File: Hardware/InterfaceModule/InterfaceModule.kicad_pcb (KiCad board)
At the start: 2 copper layers, 25 parts, among them J1 External GPS IN, J13 TS-480 COM, J14 TS-480 COM, J15 External COM, J2 External GPS OUT, J3 D-700 GPS, J4 External MIC IN, J5 D-700 MIC, J6 TS-480 MIC, J7 D-700 EXT.SP 1, J8 TS-480 EXT.SP, K1 4PDT Relay, K10 3PDT Relay, K11 3PDT Relay, K12 3PDT Relay, K13 3PDT Relay, K14 3PDT Relay, K2 4PDT Relay, K3 4PDT Relay, K4 4PDT Relay, K5 3PDT Relay, K6 3PDT Relay, K7 3PDT Relay, K8 3PDT Relay, K9 3PDT Relay

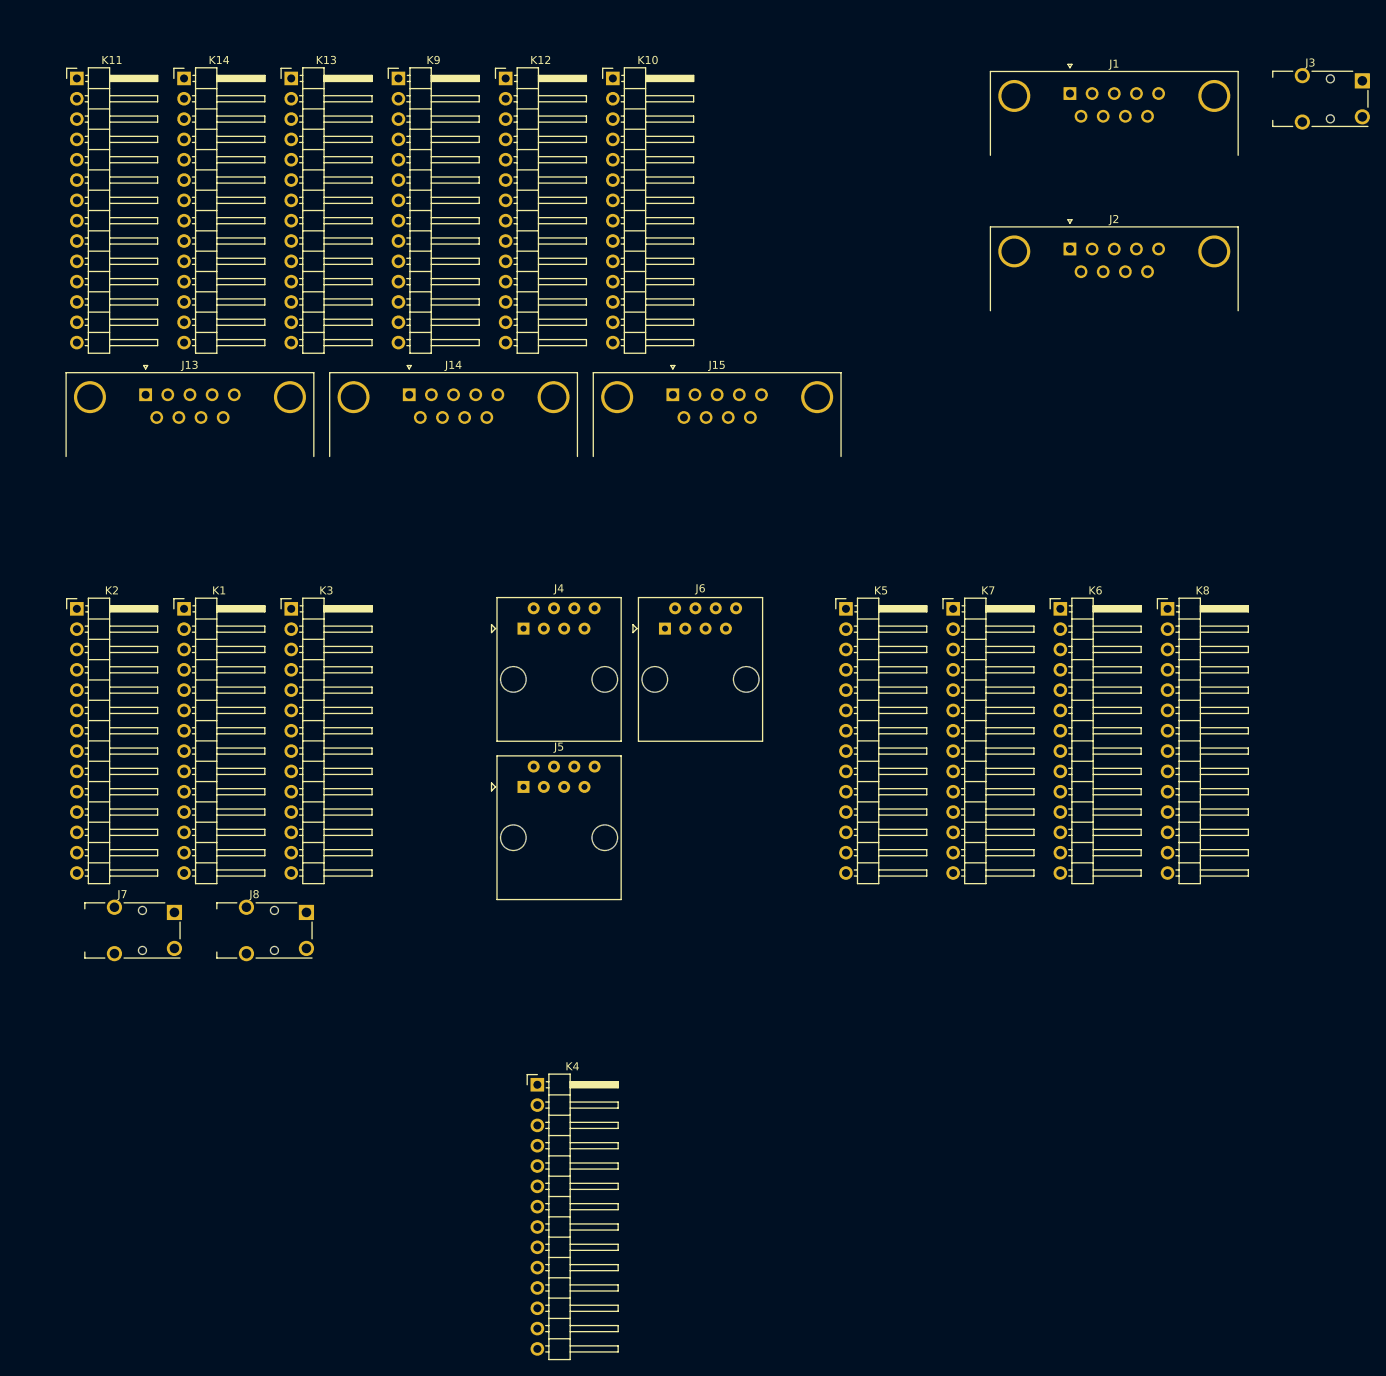
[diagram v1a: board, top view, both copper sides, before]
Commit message: Added selector input
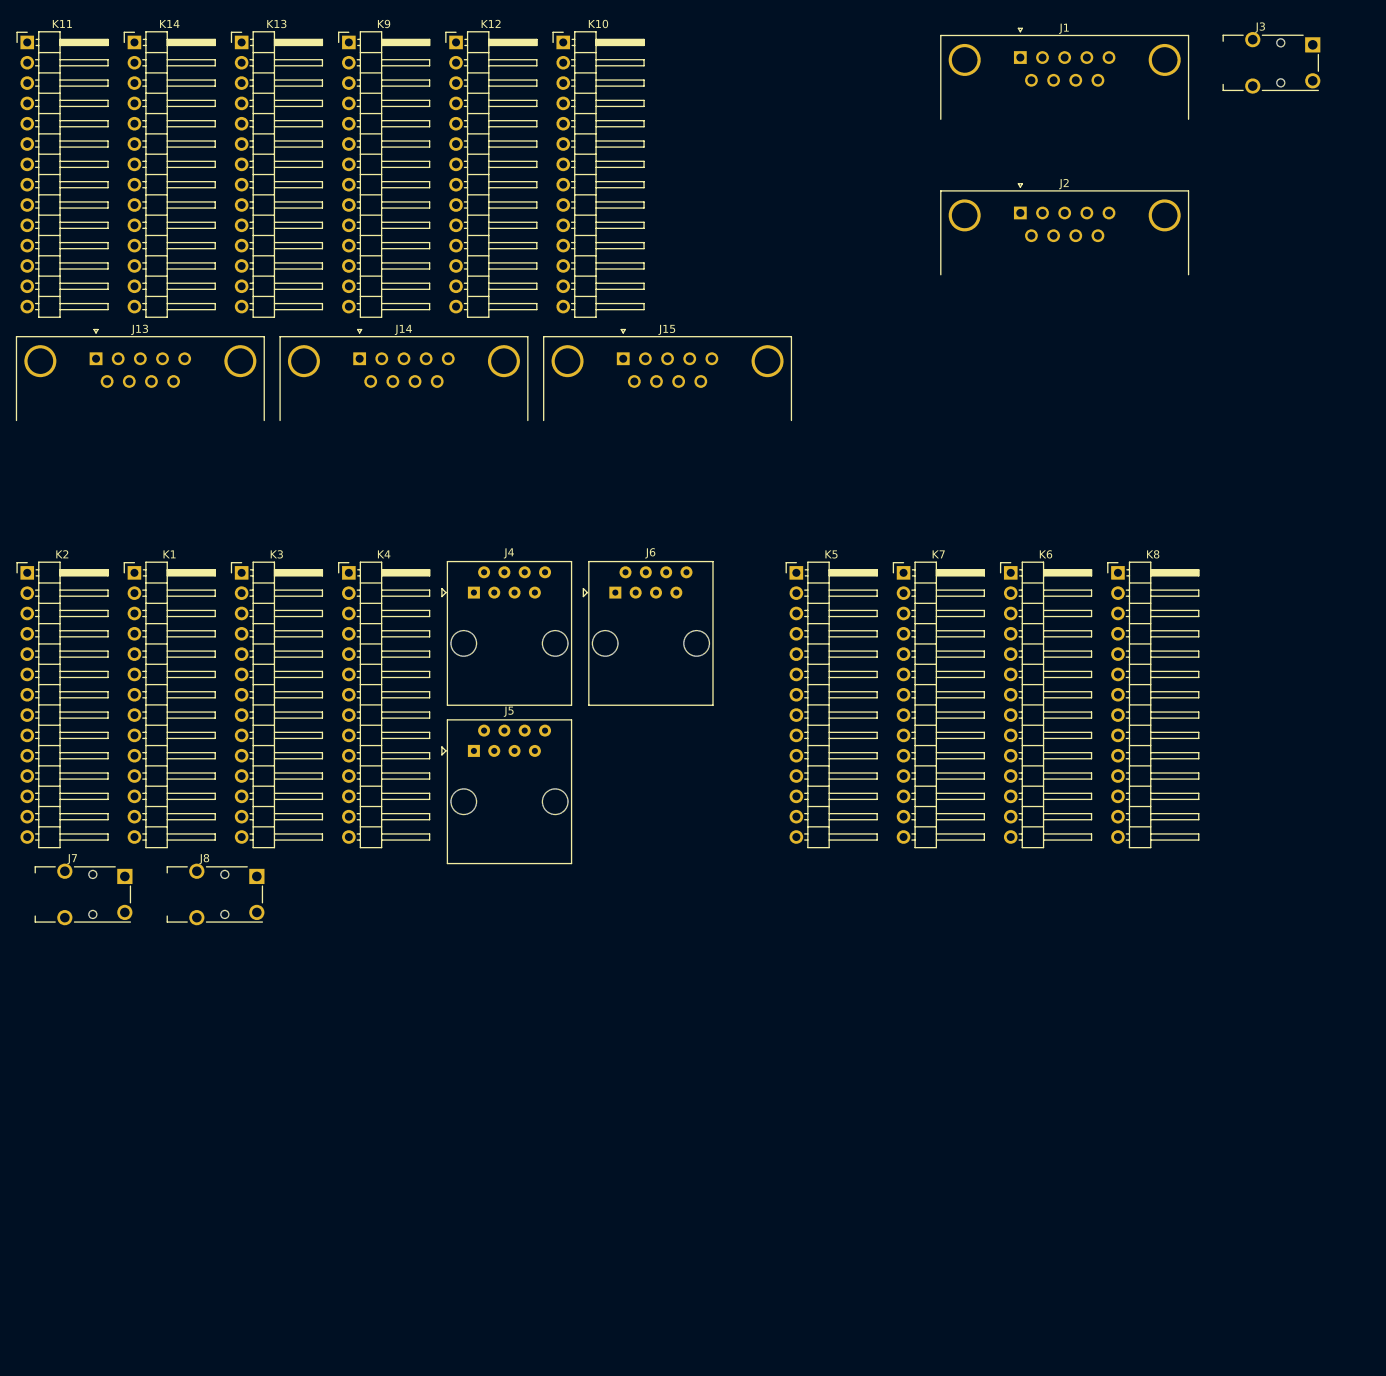
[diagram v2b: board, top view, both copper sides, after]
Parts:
- removed the J13 at (67.5, 88.5)
- added J14: TS-480 COM, Connector_Dsub:DSUB-9_Male_Horizontal_P2.77x2.84mm_EdgePinOffset4.94mm_Housed_MountingHolesOffset7.48mm, F.Cu at (94.2, 84.0)
- moved K4 68.2 mm to (92.9, 110.8)
- moved J13 39.4 mm to (61.3, 84.0)
- moved J15 7.66 mm to (127.2, 84.0)
- moved J3 7.66 mm to (206.8, 47.1)
- moved K6 7.66 mm to (175.6, 110.8)
- moved K7 7.66 mm to (162.2, 110.8)
- moved J6 7.66 mm to (126.2, 113.3)
- moved J7 7.66 mm to (58.4, 151.0)
- moved J8 7.66 mm to (74.9, 151.0)
- moved K1 7.66 mm to (66.1, 110.8)
- moved K10 7.66 mm to (119.7, 44.5)
- moved K11 7.66 mm to (52.7, 44.5)
- moved K13 7.66 mm to (79.5, 44.5)
- moved K14 7.66 mm to (66.1, 44.5)
- moved K2 7.66 mm to (52.7, 110.8)
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- renumbered J14 to J13
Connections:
- net /Data Port Switching/DATA_ANG renamed /Data Port Switching/480_DATA_ANG
- net /Data Port Switching/DATA_ANI renamed /Data Port Switching/480_DATA_ANI
- net /Data Port Switching/DATA_ANO renamed /Data Port Switching/480_DATA_ANO
- net /Data Port Switching/DATA_DE renamed /Data Port Switching/D700_DATA_DE
- net /Data Port Switching/DATA_DTS renamed /Data Port Switching/480_DATA_DTS
- net /Data Port Switching/DATA_NC renamed /Data Port Switching/480_DATA_NC
- net /Data Port Switching/DATA_PKD renamed /Data Port Switching/D700_DATA_PKD
- net /Data Port Switching/DATA_PKS renamed /Data Port Switching/D700_DATA_PKS
- net /Data Port Switching/DATA_PR1 renamed /Data Port Switching/D700_DATA_PR1
- net /Data Port Switching/DATA_PR9 renamed /Data Port Switching/D700_DATA_PR9
- J13 pad 1: /COM Port Switching/NC1 -> /COM Port Switching/480_NC1
- J13 pad 2: /COM Port Switching/RX -> /COM Port Switching/480_RX
- J13 pad 3: /COM Port Switching/TX -> /COM Port Switching/480_TX
- J13 pad 4: /COM Port Switching/DTR -> /COM Port Switching/480_DTR
- J13 pad 5: GND -> /COM Port Switching/480_GND
- J13 pad 6: /COM Port Switching/DSR -> /COM Port Switching/480_DSR
- J13 pad 7: /COM Port Switching/RTS -> /COM Port Switching/480_RTS
- J13 pad 8: /COM Port Switching/CTS -> /COM Port Switching/480_CTS
- J13 pad 9: /COM Port Switching/NC2 -> /COM Port Switching/480_NC2
- J15 pad 1: /COM Port Switching/NC1 -> /COM Port Switching/EXT_NC1
- J15 pad 2: /COM Port Switching/RX -> /COM Port Switching/EXT_RX
- J15 pad 3: /COM Port Switching/TX -> /COM Port Switching/EXT_TX
- J15 pad 4: /COM Port Switching/DTR -> /COM Port Switching/EXT_DTR
- J15 pad 5: GND -> /COM Port Switching/EXT_GND
- J15 pad 6: /COM Port Switching/DSR -> /COM Port Switching/EXT_DSR
- J15 pad 7: /COM Port Switching/RTS -> /COM Port Switching/EXT_RTS
- J15 pad 8: /COM Port Switching/CTS -> /COM Port Switching/EXT_CTS
- J15 pad 9: /COM Port Switching/NC2 -> /COM Port Switching/EXT_NC2
- J4 pad 1: /Microphone Switching/UP -> /Microphone Switching/EXT_UP
- J4 pad 2: /Microphone Switching/8V -> /Microphone Switching/EXT_8V
- J4 pad 3: GND -> /Microphone Switching/EXT_GND
- J4 pad 4: /Microphone Switching/PTT -> /Microphone Switching/EXT_PTT
- J4 pad 5: /Microphone Switching/MICGND -> /Microphone Switching/EXT_MICGND
- J4 pad 6: /Microphone Switching/MIC -> /Microphone Switching/EXT_MIC
- J4 pad 7: /Microphone Switching/NC -> /Microphone Switching/EXT_NC
- J4 pad 8: /Microphone Switching/DWN -> /Microphone Switching/EXT_DWN
- J5 pad 1: /Microphone Switching/UP -> /Microphone Switching/D700_UP
- J5 pad 2: /Microphone Switching/8V -> /Microphone Switching/D700_8V
- J5 pad 3: GND -> /Microphone Switching/D700_GND
- J5 pad 4: /Microphone Switching/PTT -> /Microphone Switching/D700_PTT
- J5 pad 5: /Microphone Switching/MICGND -> /Microphone Switching/D700_MICGND
- J5 pad 6: /Microphone Switching/MIC -> /Microphone Switching/D700_MIC
- J5 pad 7: /Microphone Switching/NC -> /Microphone Switching/D700_NC
- J5 pad 8: /Microphone Switching/DWN -> /Microphone Switching/D700_DWN
- J6 pad 1: /Microphone Switching/UP -> /Microphone Switching/480_UP
- J6 pad 2: /Microphone Switching/8V -> /Microphone Switching/480_8V
- J6 pad 3: GND -> /Microphone Switching/480_GND
- J6 pad 4: /Microphone Switching/PTT -> /Microphone Switching/480_PTT
- J6 pad 5: /Microphone Switching/MICGND -> /Microphone Switching/480_MICGND
- J6 pad 6: /Microphone Switching/MIC -> /Microphone Switching/480_MIC
- J6 pad 7: /Microphone Switching/NC -> /Microphone Switching/480_NC
- J6 pad 8: /Microphone Switching/DWN -> /Microphone Switching/480_DWN
- J7 pad S: /Microphone Switching/SP_S -> /Microphone Switching/D700_SP_S
- J7 pad T: /Microphone Switching/SP_T -> /Microphone Switching/D700_SP_T
- J8 pad S: /Microphone Switching/SP_S -> /Microphone Switching/480_SP_S
- J8 pad T: /Microphone Switching/SP_T -> /Microphone Switching/480_SP_T
- K1 pad 11: /Microphone Switching/UP -> /Microphone Switching/D700_UP
- K1 pad 12: /Microphone Switching/8V -> /Microphone Switching/D700_8V
- K1 pad 13: GND -> /Microphone Switching/D700_GND
- K1 pad 14: /Microphone Switching/PTT -> /Microphone Switching/D700_PTT
- K1 pad 2: /Microphone Switching/UP -> /Microphone Switching/EXT_UP
- K1 pad 4: /Microphone Switching/8V -> /Microphone Switching/EXT_8V
- K1 pad 6: GND -> /Microphone Switching/EXT_GND
- K1 pad 8: /Microphone Switching/PTT -> /Microphone Switching/EXT_PTT
- K10 pad 2: /COM Port Switching/DTR -> /COM Port Switching/D700_DTR
- K10 pad 3: /COM Port Switching/DSR -> /COM Port Switching/EXT_DSR
- K10 pad 4: /COM Port Switching/DSR -> /COM Port Switching/D700_DSR
- K10 pad 5: /COM Port Switching/DTR -> /COM Port Switching/EXT_DTR
- K10 pad 6: /COM Port Switching/RX -> /COM Port Switching/D700_RX
- K10 pad 7: /COM Port Switching/TX -> /COM Port Switching/EXT_TX
- K11 pad 2: /COM Port Switching/CTS -> /COM Port Switching/480_CTS
- K11 pad 3: /COM Port Switching/RTS -> /COM Port Switching/EXT_RTS
- K11 pad 4: /COM Port Switching/RX -> /COM Port Switching/480_RX
- K11 pad 5: /COM Port Switching/TX -> /COM Port Switching/EXT_TX
- K11 pad 6: /COM Port Switching/RTS -> /COM Port Switching/480_RTS
- K11 pad 7: /COM Port Switching/CTS -> /COM Port Switching/EXT_CTS
- K12 pad 2: /COM Port Switching/RTS -> /COM Port Switching/D700_RTS
- K12 pad 3: /COM Port Switching/CTS -> /COM Port Switching/EXT_CTS
- K12 pad 4: /COM Port Switching/TX -> /COM Port Switching/D700_TX
- K12 pad 5: /COM Port Switching/RX -> /COM Port Switching/EXT_RX
- K12 pad 6: /COM Port Switching/CTS -> /COM Port Switching/D700_CTS
- K12 pad 7: /COM Port Switching/RTS -> /COM Port Switching/EXT_RTS
- K13 pad 2: /COM Port Switching/NC1 -> /COM Port Switching/480_NC1
- K13 pad 3: /COM Port Switching/NC1 -> /COM Port Switching/EXT_NC1
- K13 pad 4: /COM Port Switching/NC2 -> /COM Port Switching/480_NC2
- K13 pad 5: /COM Port Switching/NC2 -> /COM Port Switching/EXT_NC2
- K13 pad 6: GND -> /COM Port Switching/480_GND
- K13 pad 7: GND -> /COM Port Switching/EXT_GND
- K14 pad 2: /COM Port Switching/NC1 -> /COM Port Switching/D700_NC1
- K14 pad 3: /COM Port Switching/NC1 -> /COM Port Switching/EXT_NC1
- K14 pad 4: /COM Port Switching/NC2 -> /COM Port Switching/D700_NC2
- K14 pad 5: /COM Port Switching/NC2 -> /COM Port Switching/EXT_NC2
- K14 pad 6: GND -> /COM Port Switching/D700_GND
- K14 pad 7: GND -> /COM Port Switching/EXT_GND
- K2 pad 11: /Microphone Switching/PTT -> /Microphone Switching/480_PTT
- K2 pad 12: GND -> /Microphone Switching/480_GND
- K2 pad 13: /Microphone Switching/8V -> /Microphone Switching/480_8V
- K2 pad 14: /Microphone Switching/UP -> /Microphone Switching/480_UP
- K2 pad 3: /Microphone Switching/PTT -> /Microphone Switching/EXT_PTT
- K2 pad 5: GND -> /Microphone Switching/EXT_GND
- K2 pad 7: /Microphone Switching/8V -> /Microphone Switching/EXT_8V
- K2 pad 9: /Microphone Switching/UP -> /Microphone Switching/EXT_UP
- K3 pad 11: /Microphone Switching/MICGND -> /Microphone Switching/D700_MICGND
- K3 pad 12: /Microphone Switching/MIC -> /Microphone Switching/D700_MIC
- K3 pad 13: /Microphone Switching/NC -> /Microphone Switching/D700_NC
- K3 pad 14: /Microphone Switching/DWN -> /Microphone Switching/D700_DWN
- K3 pad 2: /Microphone Switching/MICGND -> /Microphone Switching/EXT_MICGND
- K3 pad 3: /Microphone Switching/SP_T -> /Microphone Switching/480_SP_T
- K3 pad 4: /Microphone Switching/MIC -> /Microphone Switching/EXT_MIC
- K3 pad 6: /Microphone Switching/NC -> /Microphone Switching/EXT_NC
- K3 pad 8: /Microphone Switching/DWN -> /Microphone Switching/EXT_DWN
- K4 pad 11: /Microphone Switching/DWN -> /Microphone Switching/480_DWN
- K4 pad 12: /Microphone Switching/NC -> /Microphone Switching/480_NC
- K4 pad 13: /Microphone Switching/MIC -> /Microphone Switching/480_MIC
- K4 pad 14: /Microphone Switching/MICGND -> /Microphone Switching/480_MICGND
- K4 pad 3: /Microphone Switching/DWN -> /Microphone Switching/EXT_DWN
- K4 pad 5: /Microphone Switching/NC -> /Microphone Switching/EXT_NC
- K4 pad 7: /Microphone Switching/MIC -> /Microphone Switching/EXT_MIC
- K4 pad 8: /Microphone Switching/SP_T -> /Microphone Switching/D700_SP_T
- K4 pad 9: /Microphone Switching/MICGND -> /Microphone Switching/EXT_MICGND
- K5 pad 3: /Data Port Switching/RADIO_4 -> /Data Port Switching/SignaLink2_RADIO_4
- K5 pad 5: /Data Port Switching/RADIO_1 -> /Data Port Switching/SignaLink2_RADIO_1
- K5 pad 7: /Data Port Switching/RADIO_5 -> /Data Port Switching/SignaLink2_RADIO_5
- K6 pad 3: /Data Port Switching/RADIO_0 -> /Data Port Switching/SignaLink1_RADIO_0
- K6 pad 5: /Data Port Switching/RADIO_1 -> /Data Port Switching/SignaLink1_RADIO_1
- K6 pad 6: /Data Port Switching/DATA_SQC -> /Data Port Switching/D700_DATA_SQC
- K6 pad 7: /Data Port Switching/RADIO_2 -> /Data Port Switching/SignaLink1_RADIO_2
- K7 pad 3: /Data Port Switching/RADIO_3 -> /Data Port Switching/SignaLink2_RADIO_3
- K7 pad 5: /Data Port Switching/RADIO_0 -> /Data Port Switching/SignaLink2_RADIO_0
- K7 pad 6: /Data Port Switching/DATA_SQC -> /Data Port Switching/480_DATA_SQC
- K7 pad 7: /Data Port Switching/RADIO_2 -> /Data Port Switching/SignaLink2_RADIO_2
- K8 pad 3: /Data Port Switching/RADIO_3 -> /Data Port Switching/SignaLink1_RADIO_3
- K8 pad 5: /Data Port Switching/RADIO_4 -> /Data Port Switching/SignaLink1_RADIO_4
- K8 pad 7: /Data Port Switching/RADIO_5 -> /Data Port Switching/SignaLink1_RADIO_5
- K9 pad 2: /COM Port Switching/DSR -> /COM Port Switching/480_DSR
- K9 pad 3: /COM Port Switching/DTR -> /COM Port Switching/EXT_DTR
- K9 pad 4: /COM Port Switching/DTR -> /COM Port Switching/480_DTR
- K9 pad 5: /COM Port Switching/DSR -> /COM Port Switching/EXT_DSR
- K9 pad 6: /COM Port Switching/TX -> /COM Port Switching/480_TX
- K9 pad 7: /COM Port Switching/RX -> /COM Port Switching/EXT_RX

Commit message: Broke out switching to individual boards
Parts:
- added J10: External MIC IN, Connector_RJ:RJ45_Ninigi_GE, F.Cu at (177.8, 79.1)
- added J11: TS-480 DATA, libraries:Connector_Mini-DIN_Female_6Pin_2rows, F.Cu at (457.7, 104.4)
- added J12: D-700 DATA, libraries:Connector_Mini-DIN_Female_6Pin_2rows, F.Cu at (457.6, 142.2)
- added J16: TS-480 COM, Connector_Dsub:DSUB-9_Male_Horizontal_P2.77x2.84mm_EdgePinOffset7.70mm_Housed_MountingHolesOffset9.12mm, F.Cu at (390.4, -14.3)
- added J17: External COM, Connector_Dsub:DSUB-9_Male_Horizontal_P2.77x2.84mm_EdgePinOffset7.70mm_Housed_MountingHolesOffset9.12mm, F.Cu at (361.0, -9.70)
- added J9: TS-480 EXT.SP, libraries:Mystery_3.5mm, F.Cu at (218.7, 112.0)
- added K15: FINDER-40.52, Relay_THT:Relay_DPDT_Finder_30.22, F.Cu at (363.6, -30.1)
- added K16: FINDER-40.52, Relay_THT:Relay_DPDT_Finder_30.22, F.Cu at (366.7, -16.4)
- added K17: FINDER-40.52, Relay_THT:Relay_DPDT_Finder_30.22, F.Cu at (366.7, -5.76)
- added K18: FINDER-40.52, Relay_THT:Relay_DPDT_Finder_30.22, F.Cu at (366.7, 15.5)
- added K19: FINDER-40.52, Relay_THT:Relay_DPDT_Finder_30.22, F.Cu at (366.7, 4.90)
- added K20: FINDER-40.52, Relay_THT:Relay_DPDT_Finder_30.22, F.Cu at (366.7, 26.1)
- added K21: FINDER-40.52, Relay_THT:Relay_DPDT_Finder_30.22, F.Cu at (363.6, 14.4)
- added K22: FINDER-40.52, Relay_THT:Relay_DPDT_Finder_30.22, F.Cu at (366.7, -27.0)
- added R1: 3.9Ohm, Resistor_THT:R_Axial_DIN0204_L3.6mm_D1.6mm_P2.54mm_Vertical, F.Cu at (205.5, 102.9)
- added R2: 3.9Ohm, Resistor_THT:R_Axial_DIN0204_L3.6mm_D1.6mm_P2.54mm_Vertical, F.Cu at (205.2, 114.3)
- added R3: 470Ohm, Resistor_THT:R_Axial_DIN0204_L3.6mm_D1.6mm_P2.54mm_Vertical, F.Cu at (208.0, 102.9)
- added R4: 470Ohm, Resistor_THT:R_Axial_DIN0204_L3.6mm_D1.6mm_P2.54mm_Vertical, F.Cu at (208.0, 114.3)
- J1: value External GPS IN -> Selector Knob Connector; footprint Connector_Dsub:DSUB-9_Male_Horizontal_P2.77x2.84mm_EdgePinOffset4.94mm_Housed_MountingHolesOffset7.48mm -> Connector_RJ:RJ45_Ninigi_GE
- J13: value TS-480 COM -> SignaLink 2 RADIO; footprint Connector_Dsub:DSUB-9_Male_Horizontal_P2.77x2.84mm_EdgePinOffset4.94mm_Housed_MountingHolesOffset7.48mm -> Connector_RJ:RJ45_Ninigi_GE
- J14: value TS-480 COM -> SignaLink 1 RADIO; footprint Connector_Dsub:DSUB-9_Male_Horizontal_P2.77x2.84mm_EdgePinOffset4.94mm_Housed_MountingHolesOffset7.48mm -> Connector_RJ:RJ45_Ninigi_GE
- J15: value External COM -> D-700 COM; footprint Connector_Dsub:DSUB-9_Male_Horizontal_P2.77x2.84mm_EdgePinOffset4.94mm_Housed_MountingHolesOffset7.48mm -> Connector_Dsub:DSUB-9_Male_Horizontal_P2.77x2.84mm_EdgePinOffset7.70mm_Housed_MountingHolesOffset9.12mm
- J2: value External GPS OUT -> KrakenSDR Relay Enable; footprint Connector_Dsub:DSUB-9_Male_Horizontal_P2.77x2.84mm_EdgePinOffset4.94mm_Housed_MountingHolesOffset7.48mm -> TerminalBlock_Phoenix:TerminalBlock_Phoenix_MKDS-1,5-2_1x02_P5.00mm_Horizontal
- J3: value D-700 GPS -> External GPS IN; footprint Connector_Audio:Jack_3.5mm_Switronic_ST-005-G_horizontal -> Connector_Dsub:DSUB-9_Male_Horizontal_P2.77x2.84mm_EdgePinOffset7.70mm_Housed_MountingHolesOffset9.12mm
- J4: value External MIC IN -> External GPS OUT; footprint Connector_RJ:RJ45_Amphenol_54602-x08_Horizontal -> Connector_Dsub:DSUB-9_Male_Horizontal_P2.77x2.84mm_EdgePinOffset7.70mm_Housed_MountingHolesOffset9.12mm
- J5: value D-700 MIC -> D-700 GPS; footprint Connector_RJ:RJ45_Amphenol_54602-x08_Horizontal -> libraries:Mystery_3.5mm
- J6: value TS-480 MIC -> D-700 MIC; footprint Connector_RJ:RJ45_Amphenol_54602-x08_Horizontal -> Connector_RJ:RJ45_Ninigi_GE
- J7: value D-700 EXT.SP 1 -> TS-480 MIC; footprint Connector_Audio:Jack_3.5mm_Switronic_ST-005-G_horizontal -> Connector_RJ:RJ45_Ninigi_GE
- J8: value TS-480 EXT.SP -> D-700 EXT.SP 1; footprint Connector_Audio:Jack_3.5mm_Switronic_ST-005-G_horizontal -> libraries:Mystery_3.5mm
- K1, K2, K3, K4: value 4PDT Relay -> FINDER-40.52; footprint Connector_PinHeader_2.54mm:PinHeader_1x14_P2.54mm_Horizontal -> Relay_THT:Relay_DPDT_Finder_30.22
- K10, K11, K12, K13, K14, K5, K6, K7, K8, K9: value 3PDT Relay -> FINDER-40.52; footprint Connector_PinHeader_2.54mm:PinHeader_1x14_P2.54mm_Horizontal -> Relay_THT:Relay_DPDT_Finder_30.22
- moved K14 405.6 mm to (461.7, 133.5), turned to 90 degrees
- moved K11 398.0 mm to (440.5, 133.5), turned to 90 degrees
- moved K13 367.4 mm to (433.1, 144.1)
- moved J13 366.2 mm to (427.1, 101.7), turned to -90 degrees
- moved K12 356.2 mm to (451.1, 133.5), turned to 90 degrees
- moved K9 346.9 mm to (433.0, 112.7)
- moved J14 337.4 mm to (427.2, 138.6), turned to -90 degrees
- moved K10 322.7 mm to (429.8, 133.5), turned to 90 degrees
- moved J15 271.5 mm to (390.4, 17.6), turned to 90 degrees
- moved J1 236.9 mm to (-44.7, 130.4)
- moved J7 160.3 mm to (209.0, 96.4), turned to 90 degrees
- moved J2 155.0 mm to (31.9, 120.8), turned to 90 degrees
- moved J8 151.0 mm to (218.7, 105.2), turned to -90 degrees
- moved J3 139.2 mm to (110.3, 147.3), turned to -90 degrees
- moved K3 116.4 mm to (192.2, 81.9), turned to 90 degrees
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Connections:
- J1 pad 1: unconnected-(J1-Pad1) -> /Knob_Pos_1
- J1 pad 2: Net-(J1-Pad2) -> /Knob_Pos_2
- J1 pad 3: Net-(J1-Pad3) -> /Knob_Pos_1
- J1 pad 4: unconnected-(J1-Pad4) -> /Knob_Pos_1
- J1 pad 5: GND -> /Knob_Pos_1
- J13 pad 1: /COM Port Switching/480_NC1 -> /Data Port Switching/SignaLink2_RADIO_0
- J13 pad 2: /COM Port Switching/480_RX -> /Data Port Switching/SignaLink2_RADIO_1
- J13 pad 3: /COM Port Switching/480_TX -> /Data Port Switching/SignaLink2_RADIO_2
- J13 pad 4: /COM Port Switching/480_DTR -> /Data Port Switching/SignaLink2_RADIO_3
- J13 pad 5: /COM Port Switching/480_GND -> /Data Port Switching/SignaLink2_RADIO_4
- J13 pad 6: /COM Port Switching/480_DSR -> /Data Port Switching/SignaLink2_RADIO_5
- J13 pad 7: /COM Port Switching/480_RTS -> /Data Port Switching/SignaLink2_RADIO_6
- J13 pad 8: /COM Port Switching/480_CTS -> /Data Port Switching/SignaLink2_RADIO_7
- J14 pad 1: /COM Port Switching/D700_NC1 -> /Data Port Switching/SignaLink1_RADIO_0
- J14 pad 2: /COM Port Switching/D700_RX -> /Data Port Switching/SignaLink1_RADIO_1
- J14 pad 3: /COM Port Switching/D700_TX -> /Data Port Switching/SignaLink1_RADIO_2
- J14 pad 4: /COM Port Switching/D700_DTR -> /Data Port Switching/SignaLink1_RADIO_3
- J14 pad 5: /COM Port Switching/D700_GND -> /Data Port Switching/SignaLink1_RADIO_4
- J14 pad 6: /COM Port Switching/D700_DSR -> /Data Port Switching/SignaLink1_RADIO_5
- J14 pad 7: /COM Port Switching/D700_RTS -> /Data Port Switching/SignaLink1_RADIO_6
- J14 pad 8: /COM Port Switching/D700_CTS -> /Data Port Switching/SignaLink1_RADIO_7
- J15 pad 0: (no net) -> GND
- J15 pad 1: /COM Port Switching/EXT_NC1 -> /COM Port Switching/D700_NC1
- J15 pad 2: /COM Port Switching/EXT_RX -> /COM Port Switching/D700_RX
- J15 pad 3: /COM Port Switching/EXT_TX -> /COM Port Switching/D700_TX
- J15 pad 4: /COM Port Switching/EXT_DTR -> /COM Port Switching/D700_DTR
- J15 pad 5: /COM Port Switching/EXT_GND -> /COM Port Switching/D700_GND
- J15 pad 6: /COM Port Switching/EXT_DSR -> /COM Port Switching/D700_DSR
- J15 pad 7: /COM Port Switching/EXT_RTS -> /COM Port Switching/D700_RTS
- J15 pad 8: /COM Port Switching/EXT_CTS -> /COM Port Switching/D700_CTS
- J15 pad 9: /COM Port Switching/EXT_NC2 -> /COM Port Switching/D700_NC2
- J2 pad 1: unconnected-(J2-Pad1) -> +12V
- J2 pad 2: Net-(J1-Pad2) -> /Knob_Pos_1
- J4 pad 1: /Microphone Switching/EXT_UP -> unconnected-(J4-Pad1)
- J4 pad 2: /Microphone Switching/EXT_8V -> Net-(J3-Pad2)
- J4 pad 3: /Microphone Switching/EXT_GND -> Net-(J3-Pad3)
- J4 pad 4: /Microphone Switching/EXT_PTT -> unconnected-(J4-Pad4)
- J4 pad 5: /Microphone Switching/EXT_MICGND -> GND
- J4 pad 6: /Microphone Switching/EXT_MIC -> unconnected-(J4-Pad6)
- J4 pad 7: /Microphone Switching/EXT_NC -> unconnected-(J4-Pad7)
- J4 pad 8: /Microphone Switching/EXT_DWN -> unconnected-(J4-Pad8)
- J6 pad 1: /Microphone Switching/480_UP -> /Microphone Switching/D700_UP
- J6 pad 2: /Microphone Switching/480_8V -> /Microphone Switching/D700_8V
- J6 pad 3: /Microphone Switching/480_GND -> /Microphone Switching/D700_GND
- J6 pad 4: /Microphone Switching/480_PTT -> /Microphone Switching/D700_PTT
- J6 pad 5: /Microphone Switching/480_MICGND -> /Microphone Switching/D700_MICGND
- J6 pad 6: /Microphone Switching/480_MIC -> /Microphone Switching/D700_MIC
- J6 pad 7: /Microphone Switching/480_NC -> /Microphone Switching/D700_NC
- J6 pad 8: /Microphone Switching/480_DWN -> /Microphone Switching/D700_DWN
- J8 pad S: /Microphone Switching/480_SP_S -> /Microphone Switching/D700_SP_S
- J8 pad T: /Microphone Switching/480_SP_T -> /Microphone Switching/D700_SP_T
- K1 pad 11: /Microphone Switching/D700_UP -> /Microphone Switching/480_8V
- K1 pad 12: /Microphone Switching/D700_8V -> unconnected-(K1-Pad12)
- K1 pad 14: /Microphone Switching/D700_PTT -> /Microphone Switching/EXT_8V
- K10 pad 12: (no net) -> /Data Port Switching/D700_DATA_PR1
- K10 pad 14: (no net) -> /Data Port Switching/SignaLink1_RADIO_0
- K11 pad 12: (no net) -> /Data Port Switching/480_DATA_DTS
- K11 pad 14: (no net) -> /Data Port Switching/SignaLink2_RADIO_5
- K12 pad 12: (no net) -> /Data Port Switching/D700_DATA_SQC
- K12 pad 14: (no net) -> /Data Port Switching/SignaLink1_RADIO_2
- K13 pad 12: (no net) -> /Data Port Switching/480_DATA_ANO
- K13 pad 14: (no net) -> /Data Port Switching/SignaLink2_RADIO_0
- K14 pad 12: (no net) -> /Data Port Switching/D700_DATA_PKD
- K14 pad 14: (no net) -> /Data Port Switching/SignaLink1_RADIO_4
- K2 pad 11: /Microphone Switching/480_PTT -> /Microphone Switching/D700_8V
- K2 pad 12: /Microphone Switching/480_GND -> unconnected-(K2-Pad12)
- K2 pad 14: /Microphone Switching/480_UP -> /Microphone Switching/EXT_8V
- K3 pad 11: /Microphone Switching/D700_MICGND -> /Microphone Switching/480_PTT
- K3 pad 12: /Microphone Switching/D700_MIC -> unconnected-(K3-Pad12)
- K3 pad 14: /Microphone Switching/D700_DWN -> /Microphone Switching/EXT_PTT
- K4 pad 11: /Microphone Switching/480_DWN -> /Microphone Switching/D700_PTT
- K4 pad 12: /Microphone Switching/480_NC -> unconnected-(K4-Pad12)
- K4 pad 14: /Microphone Switching/480_MICGND -> /Microphone Switching/EXT_PTT
- K5 pad 11: Net-(K5-Pad11) -> /Microphone Switching/480_MIC
- K5 pad 12: (no net) -> Net-(K5-Pad12)
- K5 pad 14: (no net) -> /Microphone Switching/EXT_MIC
- K6 pad 11: Net-(K5-Pad11) -> /Microphone Switching/D700_MIC
- K6 pad 12: (no net) -> Net-(K6-Pad12)
- K6 pad 14: (no net) -> /Microphone Switching/EXT_MIC
- K7 pad 11: Net-(K7-Pad11) -> /Microphone Switching/480_DWN
- K7 pad 12: (no net) -> unconnected-(K7-Pad12)
- K7 pad 14: (no net) -> /Microphone Switching/EXT_DWN
- K8 pad 11: Net-(K7-Pad11) -> /Microphone Switching/D700_DWN
- K8 pad 12: (no net) -> unconnected-(K8-Pad12)
- K8 pad 14: (no net) -> /Microphone Switching/EXT_DWN
- K9 pad 12: (no net) -> /Data Port Switching/480_DATA_ANI
- K9 pad 14: (no net) -> /Data Port Switching/SignaLink2_RADIO_4
